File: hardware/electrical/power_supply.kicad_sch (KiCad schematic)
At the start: 27 parts, among them J1 Micro USB B, J3 JST-XH, Q1 IRLZ34N, Q2 IRLZ34N, Q3 IRLML5203, Q4 IRLML5203, U1 MCP73831-2-OT, U2 AP9101CK6, U3 MCP1700-3302E_SOT23

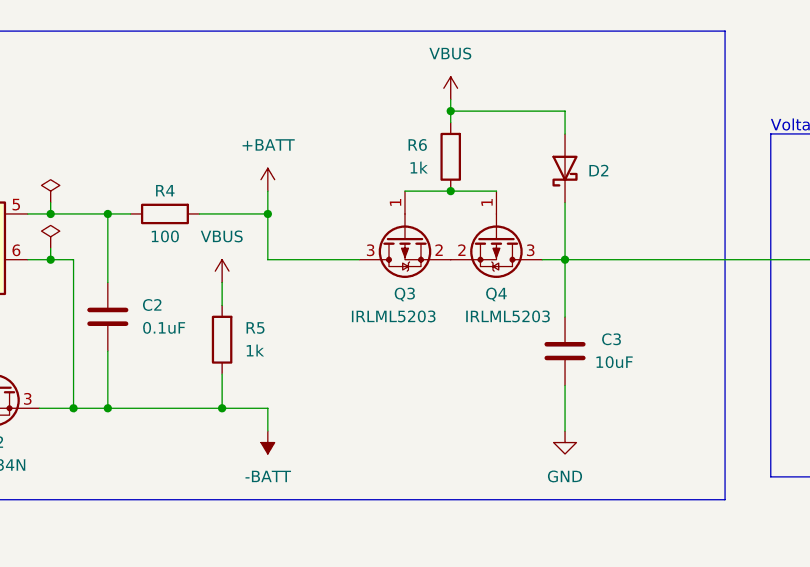
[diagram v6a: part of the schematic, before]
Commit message: PCB updated
JTC connector added; test points added; Schottky diode changed to SMD
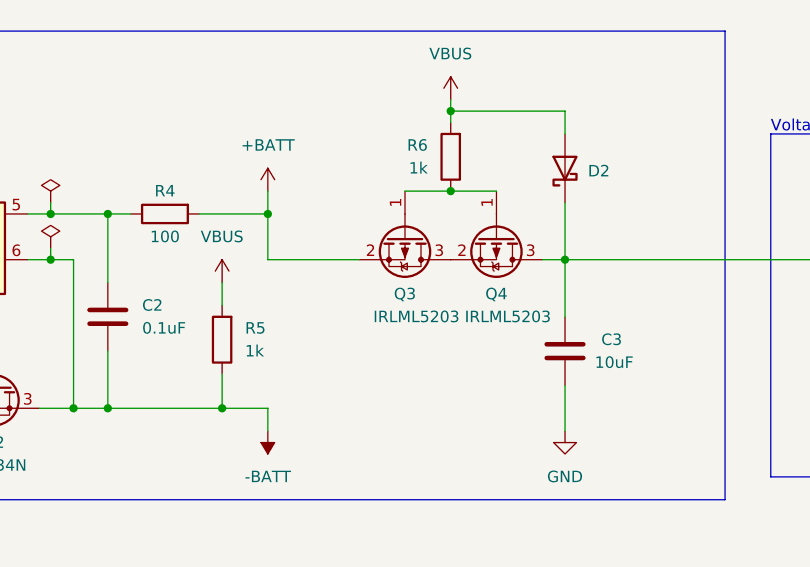
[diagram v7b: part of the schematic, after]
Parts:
- C6, C7: footprint (none) -> Capacitor_SMD:C_0402_1005Metric
- D2: footprint Diode_THT:D_DO-41_SOD81_P2.54mm_Vertical_AnodeUp -> Diode_SMD:D_SOD-323_HandSoldering
- FB1: footprint (none) -> Diode_SMD:D_0201_0603Metric
- J3: footprint Connector_PinHeader_2.00mm:PinHeader_1x02_P2.00mm_Vertical -> Connector_JST:JST_XH_S2B-XH-A-1_1x02_P2.50mm_Horizontal
- TP1, TP2: footprint (none) -> TestPoint:TestPoint_Loop_D2.50mm_Drill1.0mm_LowProfile
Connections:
- net +BATT: now also Q3.2 (S); no longer Q3.3 (D)
- net at Q4.2 (S): now also Q3.3 (D); no longer Q3.2 (S)
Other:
- moved on the sheet: Q3
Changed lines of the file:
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@@
     (property "Reference" "FB1" (id 0) (at 68.5419 116.84 90))
     (property "Value" "0R" (id 1) (at 68.5419 119.38 90))
-    (property "Footprint" "" (id 2) (at 68.58 124.968 90)
+    (property "Footprint" "Diode_SMD:D_0201_0603Metric" (id 2) (at 68.58 124.968 90)
       (effects (font (size 1.27 1.27)) hide)
     )
@@
       (effects (font (size 1.27 1.27)) (justify left) hide)
     )
-    (property "Footprint" "" (id 2) (at 67.31 102.87 0)
+    (property "Footprint" "TestPoint:TestPoint_Loop_D2.50mm_Drill1.0mm_LowProfile" (id 2) (at 67.31 102.87 0)
       (effects (font (size 1.27 1.27)) hide)
     )
@@
     (pin "1")
   )
-  (symbol (lib_id "Transistor_FET:IRLML5203") (at 184.15 48.26 90) (mirror x) (unit 1)
+  (symbol (lib_id "Transistor_FET:IRLML5203") (at 184.15 48.26 270) (unit 1)
     (in_bom yes) (on_board yes)
     (property "Reference" "Q3" (id 0) (at 184.15 54.61 90))
-    (property "Value" "IRLML5203" (id 1) (at 182.88 57.15 90))
-    (property "Footprint" "Package_TO_SOT_SMD:SOT-23" (id 2) (at 186.055 53.34 0)
+    (property "Value" "IRLML5203" (id 1) (at 185.42 57.15 90))
+    (property "Footprint" "Package_TO_SOT_SMD:SOT-23" (id 2) (at 182.245 53.34 0)
       (effects (font (size 1.27 1.27) italic) (justify left) hide)
     )
@@
       (effects (font (size 1.27 1.27)) (justify left) hide)
     )
-    (property "Footprint" "" (id 2) (at 67.31 100.33 0)
+    (property "Footprint" "TestPoint:TestPoint_Loop_D2.50mm_Drill1.0mm_LowProfile" (id 2) (at 67.31 100.33 0)
       (effects (font (size 1.27 1.27)) hide)
     )
@@
       (effects (font (size 1.27 1.27)) (justify left))
     )
-    (property "Footprint" "" (id 2) (at 64.4652 133.35 0)
+    (property "Footprint" "Capacitor_SMD:C_0402_1005Metric" (id 2) (at 64.4652 133.35 0)
       (effects (font (size 1.27 1.27)) hide)
     )
@@
     (property "Reference" "J3" (id 0) (at 46.99 88.9 0))
     (property "Value" "JST-XH" (id 1) (at 46.99 91.44 0))
-    (property "Footprint" "Connector_PinHeader_2.00mm:PinHeader_1x02_P2.00mm_Vertical" (id 2) (at 46.99 95.25 0)
+    (property "Footprint" "Connector_JST:JST_XH_S2B-XH-A-1_1x02_P2.50mm_Horizontal" (id 2) (at 46.99 95.25 0)
       (effects (font (size 1.27 1.27)) hide)
     )
@@
       (effects (font (size 1.27 1.27)) (justify right) hide)
     )
-    (property "Footprint" "Diode_THT:D_DO-41_SOD81_P2.54mm_Vertical_AnodeUp" (id 2) (at 201.93 40.64 0)
+    (property "Footprint" "Diode_SMD:D_SOD-323_HandSoldering" (id 2) (at 201.93 40.64 0)
       (effects (font (size 1.27 1.27)) hide)
     )
@@
       (effects (font (size 1.27 1.27)) (justify left))
     )
-    (property "Footprint" "" (id 2) (at 40.3352 59.69 0)
-      (effects (font (size 1.27 1.27)) hide)
-    )
+    (property "Footprint" "Capacitor_SMD:C_0402_1005Metric" (id 2) (at 40.3352 59.69 0)
+      (effects (font (size 1.27 1.27)) hide)
+    )

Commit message: corrected mistake in the original schematic
Source and drain of P-channel MOSFET Q3 were flipped
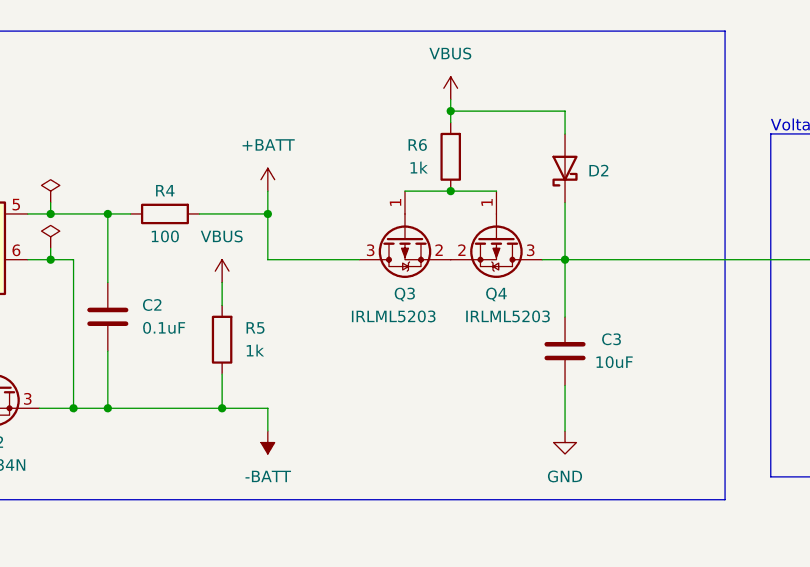
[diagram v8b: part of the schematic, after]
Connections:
- net +BATT: now also Q3.3 (D); no longer Q3.2 (S)
- net at Q4.2 (S): now also Q3.2 (S); no longer Q3.3 (D)
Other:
- moved on the sheet: Q3
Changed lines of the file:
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@@
     (pin "1")
   )
-  (symbol (lib_id "Transistor_FET:IRLML5203") (at 184.15 48.26 270) (unit 1)
+  (symbol (lib_id "Transistor_FET:IRLML5203") (at 184.15 48.26 90) (mirror x) (unit 1)
     (in_bom yes) (on_board yes)
     (property "Reference" "Q3" (id 0) (at 184.15 54.61 90))
-    (property "Value" "IRLML5203" (id 1) (at 185.42 57.15 90))
-    (property "Footprint" "Package_TO_SOT_SMD:SOT-23" (id 2) (at 182.245 53.34 0)
+    (property "Value" "IRLML5203" (id 1) (at 182.88 57.15 90))
+    (property "Footprint" "Package_TO_SOT_SMD:SOT-23" (id 2) (at 186.055 53.34 0)
       (effects (font (size 1.27 1.27) italic) (justify left) hide)
     )
